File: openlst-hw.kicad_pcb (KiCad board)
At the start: 4 copper layers, 80 x 80 mm, 166 parts, among them J1 CC Prog/Debug, J10 MS UART1, J11 EXT VBAT, J12 EXT 5V, J13 EXT VRF, J14 EXT 3V3, J15 Conn_02x24_Odd_Even, J2 UART0, J3 Control Outputs, J4 Control Outputs, J5 ANT, J6 Switch Select, J7 Conn_Coaxial, J8 MS UART0, J9 MS Prog/Debug, U1 CC1110, U10 AP63205WU, U11 AP63203WU, U12 AP63200WU, U2 MIC803, U3 SF2446E, U4 PE4250MLI, U5 PE4250MLI, U6 0433BM15A0001, U7 RFFM6406, U8 MSPM0G3107SDGS20R, U9 TJA1051TK-3, X1 TG2520SMN 27MHz

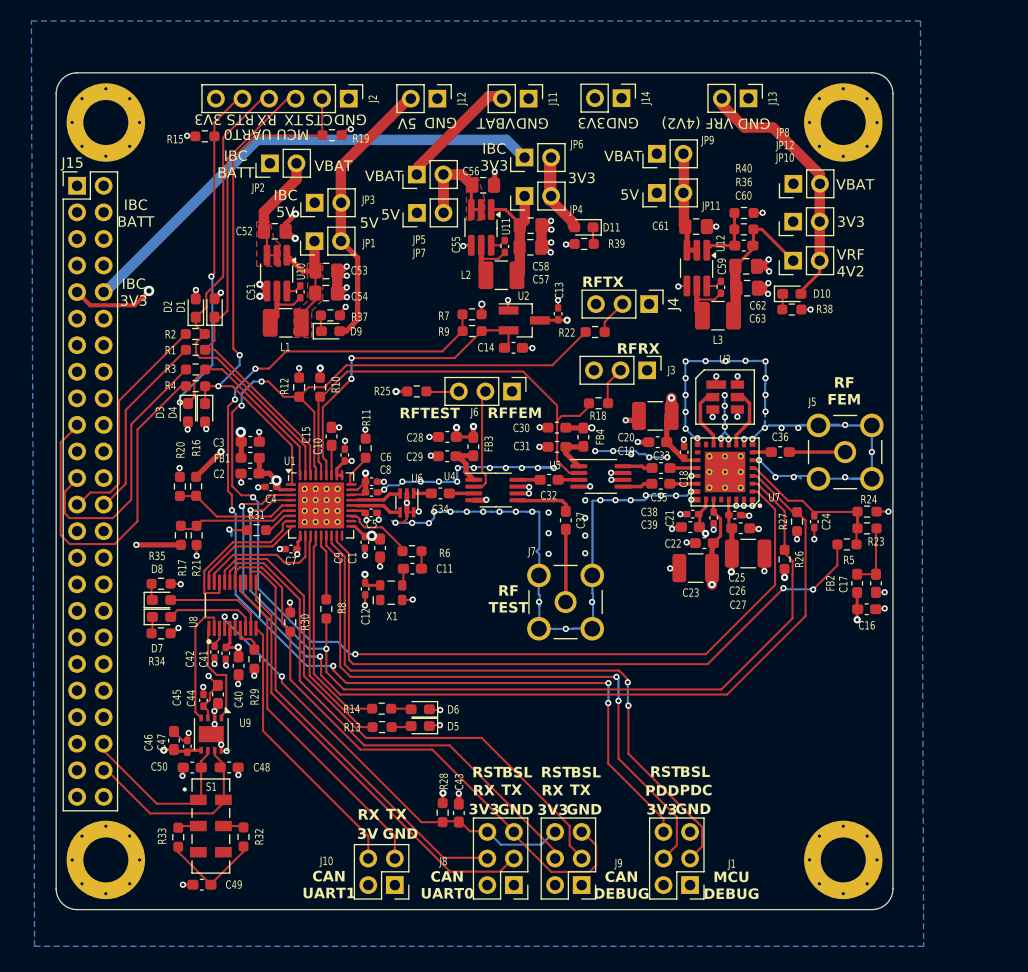
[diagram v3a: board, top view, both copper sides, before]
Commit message: use Common libraries, replace TI MCU with STM32 for CAN bridge
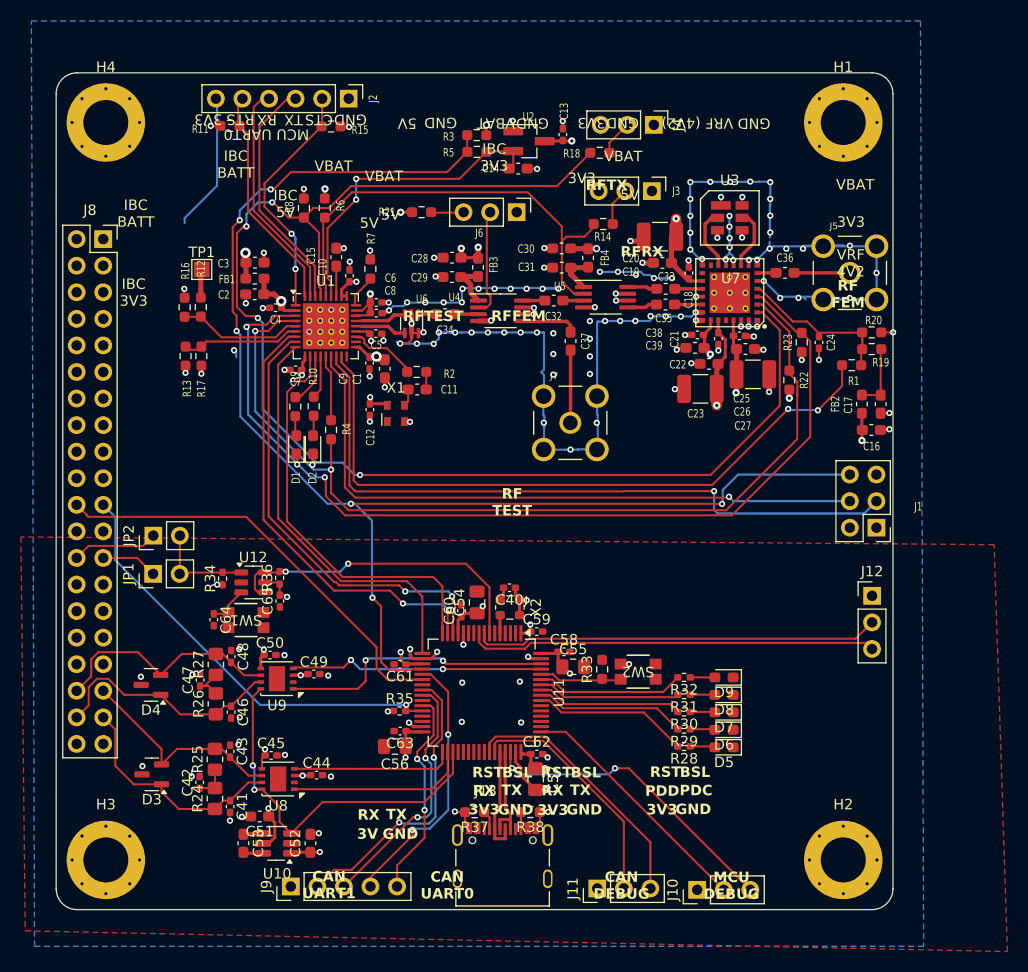
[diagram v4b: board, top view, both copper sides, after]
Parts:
- removed the D1 at (75.1, 82.5)
- removed D10, D11: GREEN, LED_SMD:LED_0603_1608Metric_Pad1.05x0.95mm_HandSolder
- removed the D2 at (73.3, 82.5)
- removed J14: EXT 3V3, Connector_PinHeader_2.54mm:PinHeader_1x02_P2.54mm_Vertical
- removed the J8 at (103.8, 137.7)
- removed JP10, JP11, JP12, JP3, JP4, JP5, JP6, JP7, JP8, JP9: Jumper_2_Open, Connector_PinHeader_2.54mm:PinHeader_1x02_P2.54mm_Vertical
- removed L1, L3: 4.7uH, Inductor_SMD:L_1210_3225Metric_Pad1.42x2.65mm_HandSolder
- removed L2: 3.9uH, Inductor_SMD:L_1210_3225Metric_Pad1.42x2.65mm_HandSolder
- removed the R1 at (73.3, 86.5)
- removed the R2 at (73.3, 85.0)
- removed the R3 at (73.3, 88.4)
- removed R39: 680, Resistor_SMD:R_0603_1608Metric_Pad0.98x0.95mm_HandSolder
- removed the R4 at (73.3, 90.0)
- removed R40: 33K, Resistor_SMD:R_0603_1608Metric_Pad0.98x0.95mm_HandSolder
- removed S1: JS202011JCQN, Project:SW_JS202011JCQN
- added C64: 100n, Capacitor_SMD:C_0402_1005Metric_Pad0.74x0.62mm_HandSolder, F.Cu at (75.1, 112.3)
- added C65: 100n, Capacitor_SMD:C_0402_1005Metric_Pad0.74x0.62mm_HandSolder, F.Cu at (81.4, 110.5)
- added D5: LED_SMD_RED, LED_SMD:LED_0603_1608Metric_Pad1.05x0.95mm_HandSolder, F.Cu at (123.8, 124.5)
- added D6: LED_SMD_GREEN, LED_SMD:LED_0603_1608Metric_Pad1.05x0.95mm_HandSolder, F.Cu at (123.8, 122.8)
- added R24: 60R4, Resistor_SMD:R_0805_2012Metric_Pad1.20x1.40mm_HandSolder, F.Cu at (75.2, 129.4)
- added R25: 60R4, Resistor_SMD:R_0805_2012Metric_Pad1.20x1.40mm_HandSolder, F.Cu at (75.2, 125.6)
- added R26: 60R4, Resistor_SMD:R_0805_2012Metric_Pad1.20x1.40mm_HandSolder, F.Cu at (75.3, 120.3)
- added R27: 60R4, Resistor_SMD:R_0805_2012Metric_Pad1.20x1.40mm_HandSolder, F.Cu at (75.3, 116.6)
- added SW1: EVP-AA602W, Common:EVP602AA, F.Cu at (78.2, 112.3)
- added SW2: EVP-AA602W, Common:EVP602AA, F.Cu at (115.6, 117.2)
- added TP1: TestPoint, TestPoint:TestPoint_Pad_1.5x1.5mm, F.Cu at (73.9, 78.8)
- added X2: 10MHz, Oscillator:Oscillator_SMD_ECS_2520MV-xxx-xx-4Pin_2.5x2.0mm, F.Cu at (103.4, 111.1)
- C40, C44: value 10u -> 100n; footprint Capacitor_SMD:C_0603_1608Metric_Pad1.08x0.95mm_HandSolder -> Capacitor_SMD:C_0402_1005Metric_Pad0.74x0.62mm_HandSolder
- C41: value 100n -> 100p
- C42: value 470n -> 4.7n
- C43: value 10n -> 100p; footprint Capacitor_SMD:C_0603_1608Metric_Pad1.08x0.95mm_HandSolder -> Capacitor_SMD:C_0402_1005Metric_Pad0.74x0.62mm_HandSolder
- C46: value 10u -> 100p; footprint Capacitor_SMD:C_0603_1608Metric_Pad1.08x0.95mm_HandSolder -> Capacitor_SMD:C_0402_1005Metric_Pad0.74x0.62mm_HandSolder
- C47: value 100n -> 4.7n
- C48: footprint Capacitor_SMD:C_0603_1608Metric_Pad1.08x0.95mm_HandSolder -> Capacitor_SMD:C_0402_1005Metric_Pad0.74x0.62mm_HandSolder
- C49: value 4n7 -> 100n; footprint Capacitor_SMD:C_0603_1608Metric_Pad1.08x0.95mm_HandSolder -> Capacitor_SMD:C_0402_1005Metric_Pad0.74x0.62mm_HandSolder
- C50, C60: value 100p -> 100n; footprint Capacitor_SMD:C_0603_1608Metric_Pad1.08x0.95mm_HandSolder -> Capacitor_SMD:C_0402_1005Metric_Pad0.74x0.62mm_HandSolder
- C51: value 100n -> 10u; footprint Capacitor_SMD:C_0402_1005Metric_Pad0.74x0.62mm_HandSolder -> Capacitor_SMD:C_0603_1608Metric_Pad1.08x0.95mm_HandSolder
- C52: footprint Capacitor_SMD:C_0805_2012Metric_Pad1.18x1.45mm_HandSolder -> Capacitor_SMD:C_0603_1608Metric_Pad1.08x0.95mm_HandSolder
- C53: value 22u -> 1u; footprint Capacitor_SMD:C_0805_2012Metric_Pad1.18x1.45mm_HandSolder -> Capacitor_SMD:C_0603_1608Metric_Pad1.08x0.95mm_HandSolder
- C54, C57: value 22u -> 10u
- C55: value 100n -> 10u; footprint Capacitor_SMD:C_0402_1005Metric_Pad0.74x0.62mm_HandSolder -> Capacitor_SMD:C_0805_2012Metric_Pad1.18x1.45mm_HandSolder
- C58, C62, C63: value 22u -> 100n; footprint Capacitor_SMD:C_0805_2012Metric_Pad1.18x1.45mm_HandSolder -> Capacitor_SMD:C_0402_1005Metric_Pad0.74x0.62mm_HandSolder
- C61: value 10u -> 100n; footprint Capacitor_SMD:C_0805_2012Metric_Pad1.18x1.45mm_HandSolder -> Capacitor_SMD:C_0402_1005Metric_Pad0.74x0.62mm_HandSolder
- D3, D4: value ESD9B5.0ST5G -> NUP2105L; footprint LED_SMD:LED_0603_1608Metric_Pad1.05x0.95mm_HandSolder -> Package_TO_SOT_SMD:SOT-23
- D7, D8: value ORANGE -> LED_SMD_YELLOW
- D9: value GREEN -> LED_SMD_YELLOW
- H1, H2, H3, H4: footprint Project:MountingHole_4.3mm_M4_Pad_Via_Custom -> Common:MountingHole_4.3mm_M4_Pad_Via_Custom
- J10: value MS UART1 -> Conn_01x03_Pin; footprint Connector_PinHeader_2.54mm:PinHeader_2x02_P2.54mm_Vertical -> Connector_PinHeader_2.54mm:PinHeader_1x03_P2.54mm_Vertical
- J11: value EXT VBAT -> Conn_01x03_Pin; footprint Connector_PinHeader_2.54mm:PinHeader_1x02_P2.54mm_Vertical -> Connector_PinHeader_2.54mm:PinHeader_1x03_P2.54mm_Vertical
- J12: value EXT 5V -> Conn_01x03_Pin; footprint Connector_PinHeader_2.54mm:PinHeader_1x02_P2.54mm_Vertical -> Connector_PinHeader_2.54mm:PinHeader_1x03_P2.54mm_Vertical
- J13: value EXT VRF -> 10155435-00011LF; footprint Connector_PinHeader_2.54mm:PinHeader_1x02_P2.54mm_Vertical -> Common:AMPHENOL_10155435-00011LF
- J5, J7: footprint Project:LINX_CONSMA001-G -> Common:LINX_CONSMA001-G
- J8: renamed from J15; value Conn_02x24_Odd_Even -> PC104 Conn_02x20_Odd_Even; footprint Connector_PinHeader_2.54mm:PinHeader_2x24_P2.54mm_Vertical -> Connector_PinSocket_2.54mm:PinSocket_2x20_P2.54mm_Vertical
- J9: value MS Prog/Debug -> Conn_01x05_Pin; footprint Connector_PinHeader_2.54mm:PinHeader_2x03_P2.54mm_Vertical -> Connector_PinHeader_2.54mm:PinHeader_1x05_P2.54mm_Vertical
- R11: renamed from R15; value 20K -> 100K
- R12: renamed from R16; value 13K7 -> DNP
- R13: renamed from R17; value 137K -> 20K
- R15: renamed from R19; value 20K -> 100K
- R16: renamed from R20; value 26K7 -> DNP
- R17: renamed from R21; value 20K -> 47K
- R28, R30: value 47K -> 680; footprint Resistor_SMD:R_0603_1608Metric_Pad0.98x0.95mm_HandSolder -> Resistor_SMD:R_0402_1005Metric_Pad0.72x0.64mm_HandSolder
- R29: value 100K -> 680; footprint Resistor_SMD:R_0603_1608Metric_Pad0.98x0.95mm_HandSolder -> Resistor_SMD:R_0402_1005Metric_Pad0.72x0.64mm_HandSolder
- R31: value 20K -> 680; footprint Resistor_SMD:R_0603_1608Metric_Pad0.98x0.95mm_HandSolder -> Resistor_SMD:R_0402_1005Metric_Pad0.72x0.64mm_HandSolder
- R32: value 60R4 -> 680; footprint Resistor_SMD:R_0603_1608Metric_Pad0.98x0.95mm_HandSolder -> Resistor_SMD:R_0402_1005Metric_Pad0.72x0.64mm_HandSolder
- R33: value 60R4 -> 10k
- R34, R35: value 680 -> 100K; footprint Resistor_SMD:R_0603_1608Metric_Pad0.98x0.95mm_HandSolder -> Resistor_SMD:R_0402_1005Metric_Pad0.72x0.64mm_HandSolder
- R36: value 165K -> 100K; footprint Resistor_SMD:R_0603_1608Metric_Pad0.98x0.95mm_HandSolder -> Resistor_SMD:R_0402_1005Metric_Pad0.72x0.64mm_HandSolder
- R37: value 1K5 -> 5K1
- R38: value 1K2 -> 5K1
- U1: footprint Project:Texas_RHH0036C_VQFN-36-1EP_6x6mm_P0.5mm_EP4.4x4.4mm_ThermalVias -> Common:Texas_RHH0036C_VQFN-36-1EP_6x6mm_P0.5mm_EP4.4x4.4mm_ThermalVias
- U10: value AP63205WU -> AP3602AKTR-G1; footprint Package_TO_SOT_SMD:TSOT-23-6_HandSoldering -> Package_TO_SOT_SMD:SOT-23-6_Handsoldering
- U11: value AP63203WU -> STM32L496RGTx; footprint Package_TO_SOT_SMD:TSOT-23-6_HandSoldering -> Package_QFP:LQFP-64_10x10mm_P0.5mm
- U12: value AP63200WU -> 74LVC2G07; footprint Package_TO_SOT_SMD:TSOT-23-6_HandSoldering -> Package_TO_SOT_SMD:SOT-23-6
- U3: footprint Project:SF2446E -> Common:SF2446E
- U7: footprint Project:RFFM6406 -> Common:RFFM6406
- U8: value MSPM0G3107SDGS20R -> TJA1042TK-3; footprint Project:DGS0020A-MFG -> Package_DFN_QFN:DFN-8-1EP_3x3mm_P0.65mm_EP1.55x2.4mm
- U9: value TJA1051TK-3 -> TJA1042TK-3
- X1: value TG2520SMN 27MHz -> 27MHz; footprint Project:Oscillator_SMD_SeikoEpson_TG2520SMN-xxx-xxxxxx-4Pin_2.5x2.0mm -> Oscillator:Oscillator_SMD_Abracon_ASDMB-4Pin_2.5x2.0mm
- moved J13 78.2 mm to (102.7, 137.1), turned to 0 degrees
- moved J11 75.8 mm to (111.7, 138.0), turned to 90 degrees
- moved J12 63.1 mm to (138.0, 110.0), turned to 0 degrees
- moved C52 58.6 mm to (84.3, 133.7), turned to 90 degrees
- moved R36 55.5 mm to (81.4, 108.3), turned to 90 degrees
- moved C53 55.3 mm to (77.9, 133.7), turned to -90 degrees
- moved D7 54.5 mm to (123.8, 121.1), turned to 180 degrees
- moved D8 54.5 mm to (123.8, 119.5), turned to 180 degrees
- moved U10 54.5 mm to (81.1, 133.7), turned to 180 degrees
- moved C56 54.3 mm to (92.4, 124.4), turned to 180 degrees
- moved R38 54.2 mm to (105.3, 130.7), turned to 180 degrees
- moved C63 53.8 mm to (92.9, 122.9), turned to 180 degrees
- moved U12 52.0 mm to (78.8, 108.7), turned to 0 degrees
- moved C57 50.8 mm to (105.8, 127.5), turned to -90 degrees
- moved C62 50.7 mm to (106.0, 125.1)
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- renumbered D5 to D1, D6 to D2, R5 to R1, R14 to R10, R18 to R14, R22 to R18, R23 to R19, R6 to R2, R24 to R20, R25 to R21, R26 to R22, R27 to R23, R7 to R3, R8 to R4, R9 to R5, R10 to R6, R11 to R7, R12 to R8, R13 to R9
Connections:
- net AN0 renamed /MCU/AN0
- net AN1 renamed /MCU/AN1
- net LST_RX_MODE renamed /MCU/LST_RX_MODE
- net LST_TX_MODE renamed /MCU/LST_TX_MODE
- net PA_VAPC renamed /MCU/PA_VAPC
- net RF_BYP renamed /MCU/RF_BYP
- net RF_EN renamed /MCU/RF_EN
- net RF_N renamed /MCU/RF_N
- net RF_P renamed /MCU/RF_P
- net UART0_RX renamed /MCU/UART0_RX
- net UART0_TX renamed /MCU/UART0_TX
- C12 pad 1: +3V3 -> /3V3_COMM
- C13 pad 2: +3V3 -> /3V3_COMM
- C16 pad 1: +3V3 -> /3V3_COMM
- C18 pad 1: +VRF -> /VRF
- C19 pad 1: +VRF -> /VRF
- C20 pad 1: +VRF -> /VRF
- C21 pad 1: +VRF -> /VRF
- C22 pad 1: +VRF -> /VRF
- C23 pad 1: +VRF -> /VRF
- C25 pad 1: +VRF -> /VRF
- C26 pad 1: +VRF -> /VRF
- C27 pad 1: +VRF -> /VRF
- C28 pad 1: +3V3 -> /3V3_COMM
- C3 pad 1: +3V3 -> /3V3_COMM
- C30 pad 1: +3V3 -> /3V3_COMM
- C38 pad 1: +3V3 -> /3V3_COMM
- C39 pad 1: +3V3 -> /3V3_COMM
- C40 pad 1: +3V3 -> /3V3_BRIDGE
- C41 pad 1: +3V3 -> /CAN Bridge/CAN2_H
- C42 pad 1: Net-(U8-VCORE) -> Net-(C42-Pad1)
- C43 pad 1: /UART-CAN/RST_N -> GND
- C43 pad 2: GND -> /CAN Bridge/CAN2_L
- C44 pad 1: +5V -> /CAN Bridge/VCC_CAN
- C45 pad 1: +5V -> /3V3_CAN
- C46 pad 1: +3V3 -> /CAN Bridge/CAN1_H
- C47 pad 1: +3V3 -> Net-(C47-Pad1)
- C48 pad 1: CAN_H -> GND
- C48 pad 2: GND -> /CAN Bridge/CAN1_L
- C49 pad 1: Net-(C49-Pad1) -> /CAN Bridge/VCC_CAN
- C50 pad 1: CAN_L -> /3V3_CAN
- C51 pad 1: Net-(U10-SW) -> /3V3_CAN
- C51 pad 2: Net-(U10-BST) -> GND
- C52 pad 1: +VBAT -> /CAN Bridge/VCC_CAN
- C53 pad 1: Net-(JP1-A) -> Net-(U10-C-)
- C53 pad 2: GND -> Net-(U10-C+)
- C54 pad 1: Net-(JP1-A) -> /3V3_BRIDGE
- C55 pad 1: Net-(U11-SW) -> /3V3_BRIDGE
- C55 pad 2: Net-(U11-BST) -> GND
- C56 pad 1: Net-(JP5-B) -> /3V3_BRIDGE
- C57 pad 1: Net-(JP4-A) -> /3V3_BRIDGE
- C58 pad 1: Net-(JP4-A) -> /3V3_BRIDGE
- C59 pad 1: Net-(U12-SW) -> /3V3_BRIDGE
- C59 pad 2: Net-(U12-BST) -> GND
- C60 pad 1: Net-(JP8-A) -> /3V3_BRIDGE
- C60 pad 2: Net-(U12-FB) -> GND
- C61 pad 1: Net-(JP11-B) -> /3V3_BRIDGE
- C62 pad 1: Net-(JP8-A) -> /3V3_BRIDGE
- C63 pad 1: Net-(JP8-A) -> /3V3_BRIDGE
- D3 pad 1: UART0_RTS -> /CAN Bridge/CAN2_H
- D3 pad 2: GND -> /CAN Bridge/CAN2_L
- D4 pad 1: UART0_CTS -> /CAN Bridge/CAN1_H
- D4 pad 2: GND -> /CAN Bridge/CAN1_L
- D7 pad 1: Net-(D7-K) -> GND
- D7 pad 2: /UART-CAN/MS_LED1 -> Net-(D7-A)
- D8 pad 1: Net-(D8-K) -> GND
- D8 pad 2: /UART-CAN/MS_LED2 -> Net-(D8-A)
- D9 pad 1: Net-(D9-K) -> GND
- D9 pad 2: +5V -> Net-(D9-A)
- FB1 pad 1: +3V3 -> /3V3_COMM
- FB2 pad 2: +3V3 -> /3V3_COMM
- FB3 pad 2: +3V3 -> /3V3_COMM
- FB4 pad 2: +3V3 -> /3V3_COMM
- J1 pad 2: +3V3 -> /3V3_COMM
- J10 pad 2: +3V3 -> /CAN Bridge/PMIC/SYS_JTMS_SWCLK
- J10 pad 3: /UART-CAN/MS_UART1_TX -> /CAN Bridge/PMIC/SYS_JTMS_SWDIO
- J11 pad 2: +VBAT -> /CAN Bridge/PMIC/USART1_RX
- J12 pad 2: +5V -> /CAN Bridge/PMIC/LPUART_RX
- J2 pad 2: UART0_CTS -> /MCU/UART0_CTS
- J2 pad 5: UART0_RTS -> /MCU/UART0_RTS
- J2 pad 6: +3V3 -> /3V3_COMM
- J3 pad 3: +3V3 -> /3V3_COMM
- J4 pad 3: +3V3 -> /3V3_COMM
- J8 pad 10: 3V3 -> /3V3_COMM
- J8 pad 11: unconnected-(J15-Pin_11-Pad11) -> /3V3_BRIDGE
- J8 pad 12: /INTERBOARD_CONNECTOR2/EPS_RESET -> /3V3_CAN
- J8 pad 13: /INTERBOARD_CONNECTOR2/3V3_9 -> /INTERBOARD_CONNECTOR2/3V3_7
- J8 pad 14: /INTERBOARD_CONNECTOR2/3V3_13 -> /INTERBOARD_CONNECTOR2/3V3_6
- J8 pad 15: /INTERBOARD_CONNECTOR2/3V3_3 -> /INTERBOARD_CONNECTOR2/3V3_9
- J8 pad 16: /INTERBOARD_CONNECTOR2/3V3_7 -> /INTERBOARD_CONNECTOR2/3V3_8
- J8 pad 17: /INTERBOARD_CONNECTOR2/UART_A_TXO -> /INTERBOARD_CONNECTOR2/3V3_5
- J8 pad 18: /INTERBOARD_CONNECTOR2/UART_A_RXI -> /INTERBOARD_CONNECTOR2/3V3_4
- J8 pad 19: /INTERBOARD_CONNECTOR2/UART_B_RTS -> /INTERBOARD_CONNECTOR2/3V3_3
- J8 pad 20: /INTERBOARD_CONNECTOR2/AVI_RESET -> /INTERBOARD_CONNECTOR2/3V3_2
- J8 pad 21: GND -> /CAN Bridge/ATTENTION
- J8 pad 22: /INTERBOARD_CONNECTOR2/3V3_12 -> /CAN Bridge/EPS_RST
- J8 pad 23: /INTERBOARD_CONNECTOR2/UART_B_CTS -> /INTERBOARD_CONNECTOR2/*SCI_RST
- J8 pad 24: GND -> /INTERBOARD_CONNECTOR2/*AVI_RST
- J8 pad 25: /INTERBOARD_CONNECTOR2/UART_B_TXO -> /CAN Bridge/COMM1_RST
- J8 pad 26: /INTERBOARD_CONNECTOR2/UART_B_RXI -> /CAN Bridge/COMM2_RST
- J8 pad 27: /INTERBOARD_CONNECTOR2/3V3_6 -> GND
- J8 pad 28: /INTERBOARD_CONNECTOR2/3V3_2 -> GND
- J8 pad 29: /INTERBOARD_CONNECTOR2/3V3_8 -> /INTERBOARD_CONNECTOR2/5V0_1
- J8 pad 3: BATT -> /INTERBOARD_CONNECTOR2/BATT_1
- J8 pad 30: /INTERBOARD_CONNECTOR2/3V3_1 -> /INTERBOARD_CONNECTOR2/5V0_2
- J8 pad 31: /INTERBOARD_CONNECTOR2/3V3_4 -> /INTERBOARD_CONNECTOR2/5V0_3
- J8 pad 32: GND -> /INTERBOARD_CONNECTOR2/5V0_4
- J8 pad 33: /INTERBOARD_CONNECTOR2/5V0_2 -> GND
- J8 pad 34: /INTERBOARD_CONNECTOR2/SCI_RST -> GND
- J8 pad 35: GND -> /CAN Bridge/CAN2_L
- J8 pad 36: GND -> /CAN Bridge/CAN1_L
- J8 pad 37: /INTERBOARD_CONNECTOR2/5V0_4 -> /CAN Bridge/CAN2_H
- J8 pad 38: /INTERBOARD_CONNECTOR2/5V0_3 -> /CAN Bridge/CAN1_H
- J8 pad 39: unconnected-(J15-Pin_39-Pad39) -> GND
- J8 pad 4: BATT -> /VRF
- J8 pad 40: /INTERBOARD_CONNECTOR2/3V3_5 -> GND
- J8 pad 5: /INTERBOARD_CONNECTOR2/3V3_11 -> GND
- J8 pad 6: /INTERBOARD_CONNECTOR2/2V8_1 -> GND
- J8 pad 7: GND -> /INTERBOARD_CONNECTOR2/3V3_1
- J8 pad 8: GND -> /INTERBOARD_CONNECTOR2/BATT
- J8 pad 9: 5V0 -> /INTERBOARD_CONNECTOR2/3V3_13
- J9 pad 2: +3V3 -> /CAN Bridge/PMIC/USART3_TX
- J9 pad 3: /UART-CAN/SWCLK -> /CAN Bridge/PMIC/USART3_RX
- J9 pad 4: /UART-CAN/SWDIO -> /CAN Bridge/PMIC/USART3_CTS
- J9 pad 5: /UART-CAN/BSL -> /CAN Bridge/PMIC/USART3_RTS
- JP1 pad 1: Net-(JP1-A) -> /CAN Bridge/COMM1_RST
- JP1 pad 2: +5V -> /CAN Bridge/PMIC/EXTR_RST
- JP2 pad 1: BATT -> /CAN Bridge/COMM2_RST
- JP2 pad 2: +VBAT -> /CAN Bridge/PMIC/EXTR_RST
- R11 pad 2: UART0_RTS -> /MCU/UART0_RTS
- R12 pad 2: +VRF -> Net-(R12-Pad2)
- R13 pad 2: +VBAT -> /VRF
- R15 pad 2: UART0_CTS -> /MCU/UART0_CTS
- R21 pad 1: +3V3 -> /3V3_COMM
- R22 pad 2: +3V3 -> /3V3_COMM
- R28 pad 1: +3V3 -> Net-(D5-A)
- R28 pad 2: /UART-CAN/RST_N -> /CAN Bridge/PMIC/LED1
- R29 pad 1: GND -> Net-(D6-A)
- R29 pad 2: Net-(U8-PA2_ROSC) -> /CAN Bridge/PMIC/LED2
- R3 pad 2: +3V3 -> /3V3_COMM
- R30 pad 1: GND -> Net-(D7-A)
- R30 pad 2: /UART-CAN/BSL -> /CAN Bridge/PMIC/LED3
- R31 pad 1: GND -> Net-(D8-A)
- R31 pad 2: UART1_CTS -> /CAN Bridge/PMIC/LED4
- R32 pad 1: Net-(C49-Pad1) -> Net-(D9-A)
- R32 pad 2: Net-(R32-Pad2) -> /CAN Bridge/PMIC/LED5
- R33 pad 1: Net-(C49-Pad1) -> Net-(U11-PH3_BOOT0)
- R33 pad 2: Net-(R33-Pad2) -> GND
- R34 pad 1: Net-(D7-K) -> /3V3_BRIDGE
- R34 pad 2: GND -> /CAN Bridge/PMIC/EXTR_RST
- R35 pad 1: Net-(D8-K) -> /3V3_BRIDGE
- R35 pad 2: GND -> /CAN Bridge/ATTENTION
- R36 pad 1: Net-(JP8-A) -> /3V3_BRIDGE
- R36 pad 2: Net-(U12-FB) -> /CAN Bridge/PMIC/Schmitt Trigger/OUT
- R37 pad 1: Net-(D9-K) -> Net-(J13-CC1_A)
- R38 pad 1: Net-(D10-K) -> GND
- R38 pad 2: GND -> Net-(J13-CC2_B)
- R6 pad 2: +3V3 -> /3V3_COMM
- U1 pad 1: UART0_CTS -> /MCU/UART0_CTS
- U1 pad 11: UART1_RX -> /CAN Bridge/UART_TX
- U1 pad 36: UART0_RTS -> /MCU/UART0_RTS
- U1 pad 7: UART1_CTS -> /CAN Bridge/UART_RTS
- U1 pad 8: UART1_RTS -> /CAN Bridge/UART_CTS
- U1 pad 9: UART1_TX -> /CAN Bridge/UART_RX
- U10 pad 1: Net-(JP1-A) -> /CAN Bridge/VCC_CAN
- U10 pad 2: +VBAT -> GND
- U10 pad 3: +VBAT -> /CAN Bridge/CAN_RS
- U10 pad 4: GND -> Net-(U10-C-)
- U10 pad 5: Net-(U10-SW) -> /3V3_CAN
- U10 pad 6: Net-(U10-BST) -> Net-(U10-C+)
- U11 pad 1: Net-(JP4-A) -> /3V3_BRIDGE
- U11 pad 2: Net-(JP5-B) -> unconnected-(U11-PC13-Pad2)
- U11 pad 3: Net-(JP5-B) -> unconnected-(U11-PC14-Pad3)
- U11 pad 4: GND -> unconnected-(U11-PC15-Pad4)
- U11 pad 5: Net-(U11-SW) -> /CAN Bridge/PMIC/HSE_IN
- U11 pad 6: Net-(U11-BST) -> unconnected-(U11-PH1-Pad6)
- U12 pad 1: Net-(U12-FB) -> /CAN Bridge/PMIC/EXTR_RST
- U12 pad 2: Net-(JP11-B) -> GND
- U12 pad 3: Net-(JP11-B) -> /CAN Bridge/PMIC/Schmitt Trigger/IN1
- U12 pad 4: GND -> /CAN Bridge/PMIC/Schmitt Trigger/OUT
- U12 pad 5: Net-(U12-SW) -> /3V3_BRIDGE
- U12 pad 6: Net-(U12-BST) -> /CAN Bridge/PMIC/Schmitt Trigger/OUT
- U2 pad 3: +3V3 -> /3V3_COMM
- U7 pad 17: +VRF -> /VRF
- U7 pad 23: +3V3 -> /3V3_COMM
- U7 pad 24: +VRF -> /VRF
- U7 pad 26: +VRF -> /VRF
- U8 pad 1: /UART-CAN/CAN_TX -> /CAN Bridge/CAN Transceiver2/CAN_TX
- U8 pad 2: /UART-CAN/CAN_RX -> GND
- U8 pad 3: Net-(U8-VCORE) -> /CAN Bridge/VCC_CAN
- U8 pad 4: /UART-CAN/RST_N -> /CAN Bridge/CAN Transceiver2/CAN_RX
- U8 pad 5: +3V3 -> /3V3_CAN
- U8 pad 6: GND -> /CAN Bridge/CAN2_L
- U8 pad 7: Net-(U8-PA2_ROSC) -> /CAN Bridge/CAN2_H
- U8 pad 8: /UART-CAN/MS_LED1 -> /CAN Bridge/CAN_RS
- U8 pad 9: /UART-CAN/MS_LED2 -> GND
- U9 pad 1: /UART-CAN/CAN_TX -> /CAN Bridge/CAN Transceiver1/CAN_TX
- U9 pad 3: +5V -> /CAN Bridge/VCC_CAN
- U9 pad 4: /UART-CAN/CAN_RX -> /CAN Bridge/CAN Transceiver1/CAN_RX
- U9 pad 5: +3V3 -> /3V3_CAN
- U9 pad 6: CAN_L -> /CAN Bridge/CAN1_L
- U9 pad 7: CAN_H -> /CAN Bridge/CAN1_H
- U9 pad 8: GND -> /CAN Bridge/CAN_RS
- X1 pad 4: +3V3 -> /3V3_COMM
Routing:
- net +5V: track 132.1 -> 0.00 mm, vias 1 -> 0
- net /VRF: track 0.00 -> 130.0 mm, vias 0 -> 4
- net +VBAT: track 127.7 -> 0.00 mm, vias 1 -> 0
- net +VRF: track 110.5 -> 0.00 mm, vias 4 -> 0
- net +3V3: track 93.2 -> 0.00 mm, vias 15 -> 0
- net /3V3_BRIDGE: track 0.00 -> 84.3 mm, vias 0 -> 11
- net /3V3_COMM: track 0.00 -> 74.4 mm, vias 0 -> 12
- net /3V3_CAN: track 0.00 -> 64.9 mm, vias 0 -> 3
- net /UART-CAN/BSL: track 56.7 -> 0.00 mm
- net /UART-CAN/SWCLK: track 53.1 -> 0.00 mm
- net UART0_CTS: track 52.6 -> 0.00 mm, vias 2 -> 0
- net UART0_RTS: track 51.6 -> 0.00 mm, vias 2 -> 0
- net /UART-CAN/SWDIO: track 49.0 -> 0.00 mm
- net 3V3: track 46.8 -> 0.00 mm
- net /UART-CAN/RST_N: track 42.8 -> 0.00 mm, vias 2 -> 0
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- added copper zone on In2.Cu, net /3V3_BRIDGE
- added copper zone on In2.Cu, net /3V3_CAN
- added copper zone on In2.Cu, net /3V3_COMM
- added copper zone on In2.Cu, net /VRF
- added copper zone on F.Cu, net GND
- removed copper zone on In2.Cu, net +3V3
- removed copper zone on F.Cu, net +VBAT
- removed copper zone on In2.Cu, net +VRF
- removed copper zone on F.Cu, net Net-(JP1-A)
- removed copper zone on F.Cu, net Net-(JP5-B)

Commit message: integrated stm32 as CAN bridge and pc104 bus
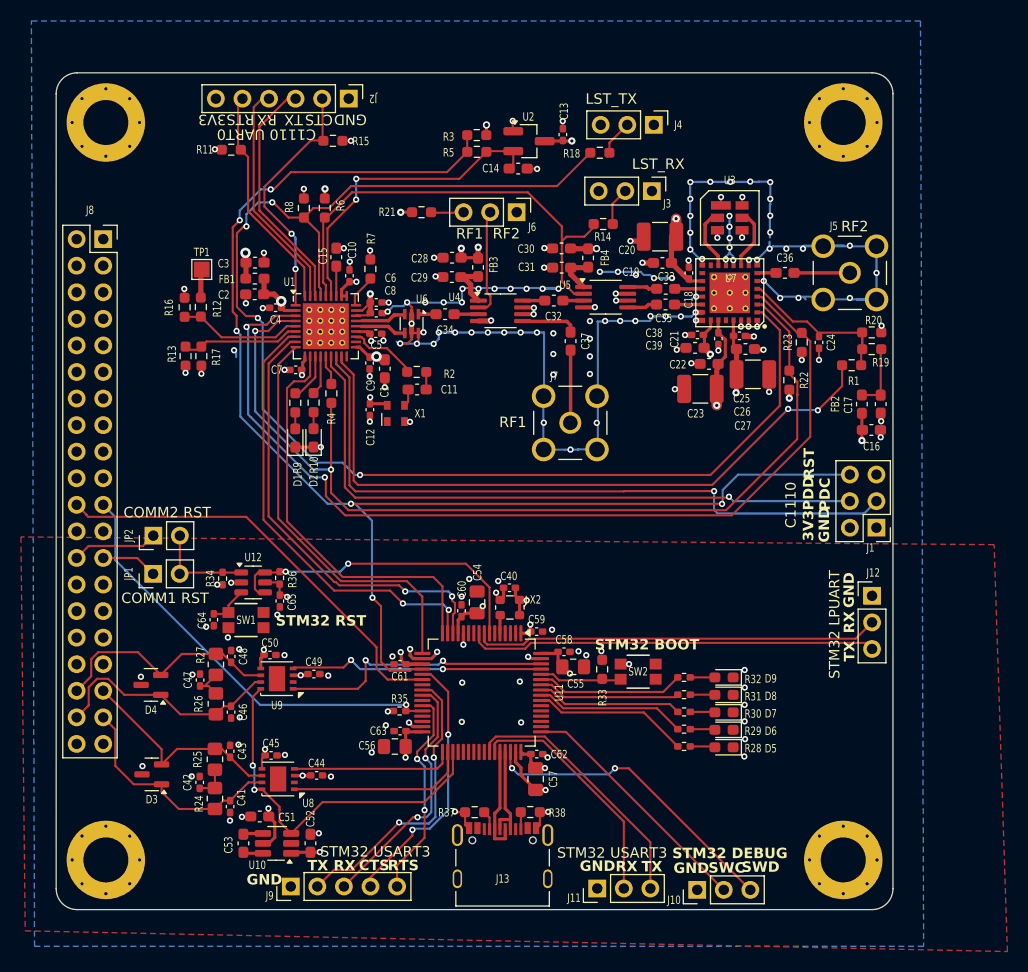
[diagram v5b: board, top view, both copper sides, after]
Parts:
- moved R4 3.48 mm to (86.3, 90.7)
- moved R11 2.28 mm to (76.7, 67.3)
- moved R15 1.38 mm to (86.5, 66.5)
- moved D2 0.67 mm to (84.6, 94.9)
- moved D1 0.66 mm to (82.9, 94.9)
- moved R9 0.37 mm to (82.9, 91.5)
- moved R10 0.35 mm to (84.6, 91.5)
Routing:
- net /3V3_COMM: track 74.4 -> 61.0 mm
- net /MCU/RF_EN: track 89.5 -> 93.0 mm
- net Net-(U1-P2_0): track 6.41 -> 2.95 mm
- net GND: track 217.5 -> 219.2 mm, vias 162 -> 182
- net /MCU/UART0_CTS: track 23.8 -> 24.4 mm
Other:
- board text added: "C1110"
- board text added: "C1110 UART0"
- board text added: "COMM1 RST"
- board text added: "COMM2 RST"
- board text added: "LST_RX"
- board text added: "LST_TX"
- board text added: "RF1"
- board text added: "RF2"
- board text added: "STM32 BOOT"
- board text added: "STM32 DEBUG"
- board text added: "STM32 LPUART"
- board text added: "STM32 RST"
- board text added: "STM32 USART3"
- board text added: "SWC"
- board text added: "SWD"
- board text removed: "3V"
- board text removed: "5V"
- board text removed: "BSL"
- board text removed: "CAN DEBUG"
- board text removed: "CAN UART0"
- board text removed: "CAN UART1"
- board text removed: "IBC 3V3"
- board text removed: "IBC 5V"
- board text removed: "IBC BATT"
- board text removed: "MCU DEBUG"
- board text removed: "MCU UART0"
- board text removed: "RF FEM"
- board text removed: "RF TEST"
- board text removed: "RFFEM"
- board text removed: "RFRX"
- board text removed: "RFTEST"
- board text removed: "RFTX"
- board text removed: "VBAT"
- board text removed: "VRF (4V2)"
- board text removed: "VRF 4V2"
